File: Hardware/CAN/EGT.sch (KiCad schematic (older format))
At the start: 1 part

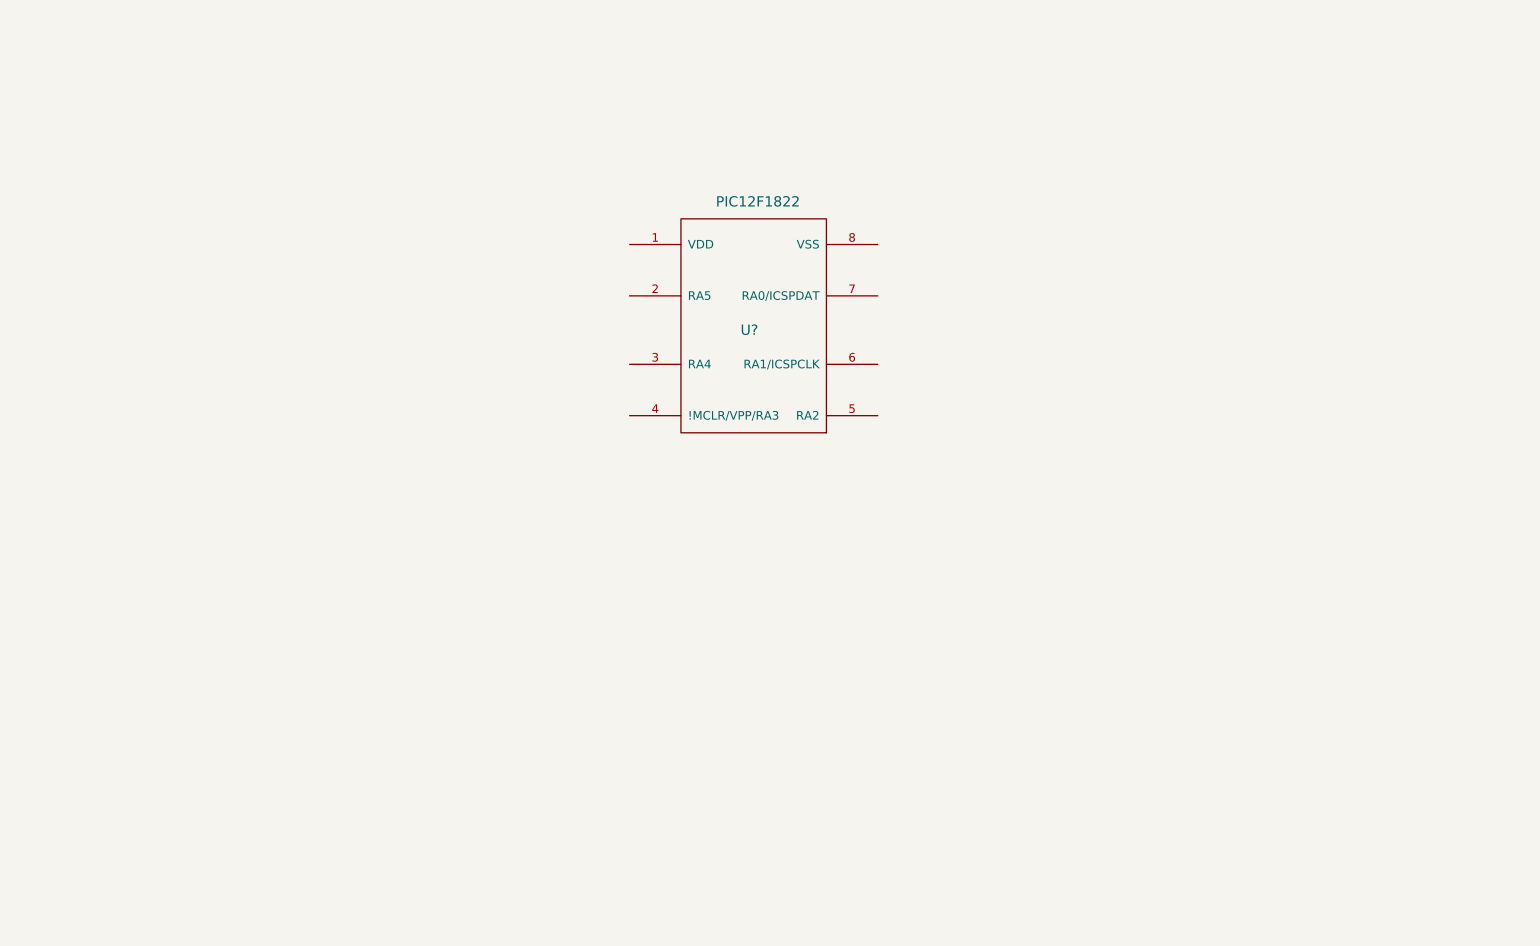
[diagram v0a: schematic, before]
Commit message: Added components, library
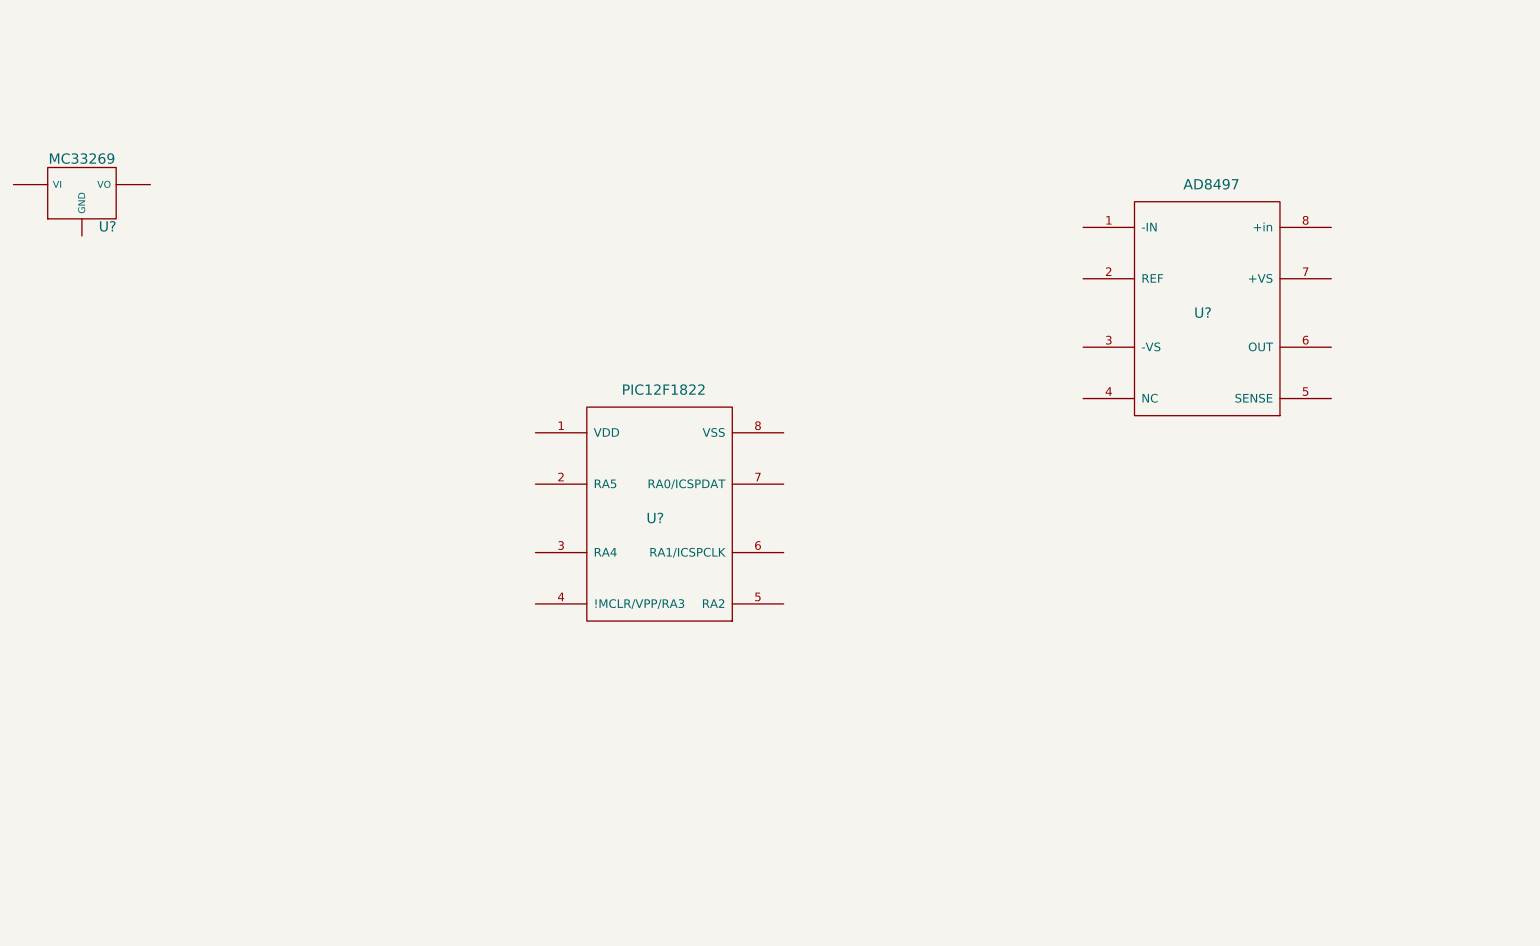
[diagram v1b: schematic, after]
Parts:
- added U?: MC33269, ~, symbol MC33269
- added U?: AD8497, ~, symbol AD8497
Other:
- moved on the sheet: U?
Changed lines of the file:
@@
 LIBS:contrib
 LIBS:valves
-LIBS:EGT-cache
 EELAYER 27 0
 EELAYER END
@@
 L PIC12F1822 U?
 U 1 1 51C7BBAD
-P 6400 3150
-F 0 "U?" H 6350 3150 60  0000 C CNN
-F 1 "PIC12F1822" H 6400 3900 60  0000 C CNN
-F 2 "" H 6400 3150 60  0000 C CNN
-F 3 "" H 6400 3150 60  0000 C CNN
-	1    6400 3150
+P 5850 4250
+F 0 "U?" H 5800 4250 60  0000 C CNN
+F 1 "PIC12F1822" H 5850 5000 60  0000 C CNN
+F 2 "" H 5850 4250 60  0000 C CNN
+F 3 "" H 5850 4250 60  0000 C CNN
+	1    5850 4250
 	1    0    0    -1
 $EndComp
+$Comp
+L MC33269 U?
+U 1 1 51C7C963
+P 2450 2350
+F 0 "U?" H 2600 2154 60  0000 C CNN
+F 1 "MC33269" H 2450 2550 60  0000 C CNN
+F 2 "~" H 2450 2350 60  0000 C CNN
+F 3 "~" H 2450 2350 60  0000 C CNN
+	1    2450 2350
+	1    0    0    -1
+$EndComp
+$Comp
+L AD8497 U?
+U 1 1 51C7CB48
+P 9050 3050
+F 0 "U?" H 9000 3050 60  0000 C CNN
+F 1 "AD8497" H 9050 3800 60  0000 C CNN
+F 2 "~" H 9050 3050 60  0000 C CNN
+F 3 "~" H 9050 3050 60  0000 C CNN
+	1    9050 3050
+	1    0    0    -1
+$EndComp

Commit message: Schematic work
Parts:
- removed U?: PIC12F1822, symbol PIC12F1822
- removed U?: AD8497, ~, symbol AD8497
- added C1, C2: 10uF, ~, symbol CAPAPOL
- added C? (x6): C, ~, symbol C
- added D1: SCHOTTKY, ~, symbol DIODESCH
- added P?: CONN_4, symbol CONN_4
- added P?: CONN_2, symbol CONN_2
- added R? (x7): R, ~, symbol R
- added U?: PIC12F1840, ~, symbol PIC12F1840
- added U?: AD8628, ~, symbol AD8628
- added U?: TJA1051TK/3, ~, symbol TJA1051TK/3
- gave numbers to parts that had none: 1
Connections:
- net at VR1.GND: now also C1.2, C2.2, C?.2, C?.2, C?.2, C?.2, C?.2, P?.2 (P2), R?.2, R?.2, U?.2 (GND), U?.4 (V-), U?.8 (S), U?.8 (VSS)
- net at VR1.VI: now also C1.1, D1.2 (K)
- net at VR1.VO: now also C2.1, C?.1, R?.1, U?.1 (VDD), U?.3 (VCC), U?.5 (VIO), U?.8 (V+)
- new net: U?.2 (RA5), U?.4 (RXD)
- new net: U?.1 (TXD), U?.3 (RA4)
- new net: C?.1, R?.1, R?.2, U?.4 (!MCLR/VPP/RA3)
- new net: C?.1, R?.2, U?.5 (RA2)
- new net: R?.1, R?.2, U?.1
- new net: C?.1, C?.2, R?.1, R?.2, U?.2 (_)
- new net: C?.1, C?.1, R?.1, R?.2, U?.3 (+)
- new net: P?.3 (P3), U?.6 (CANL)
- new net: P?.4 (P4), U?.7 (CANH)
- new net: D1.1 (A), P?.1 (P1)
- new net: P?.1 (P1), R?.1
- new net: P?.2 (PM), R?.1
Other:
- moved on the sheet: VR1

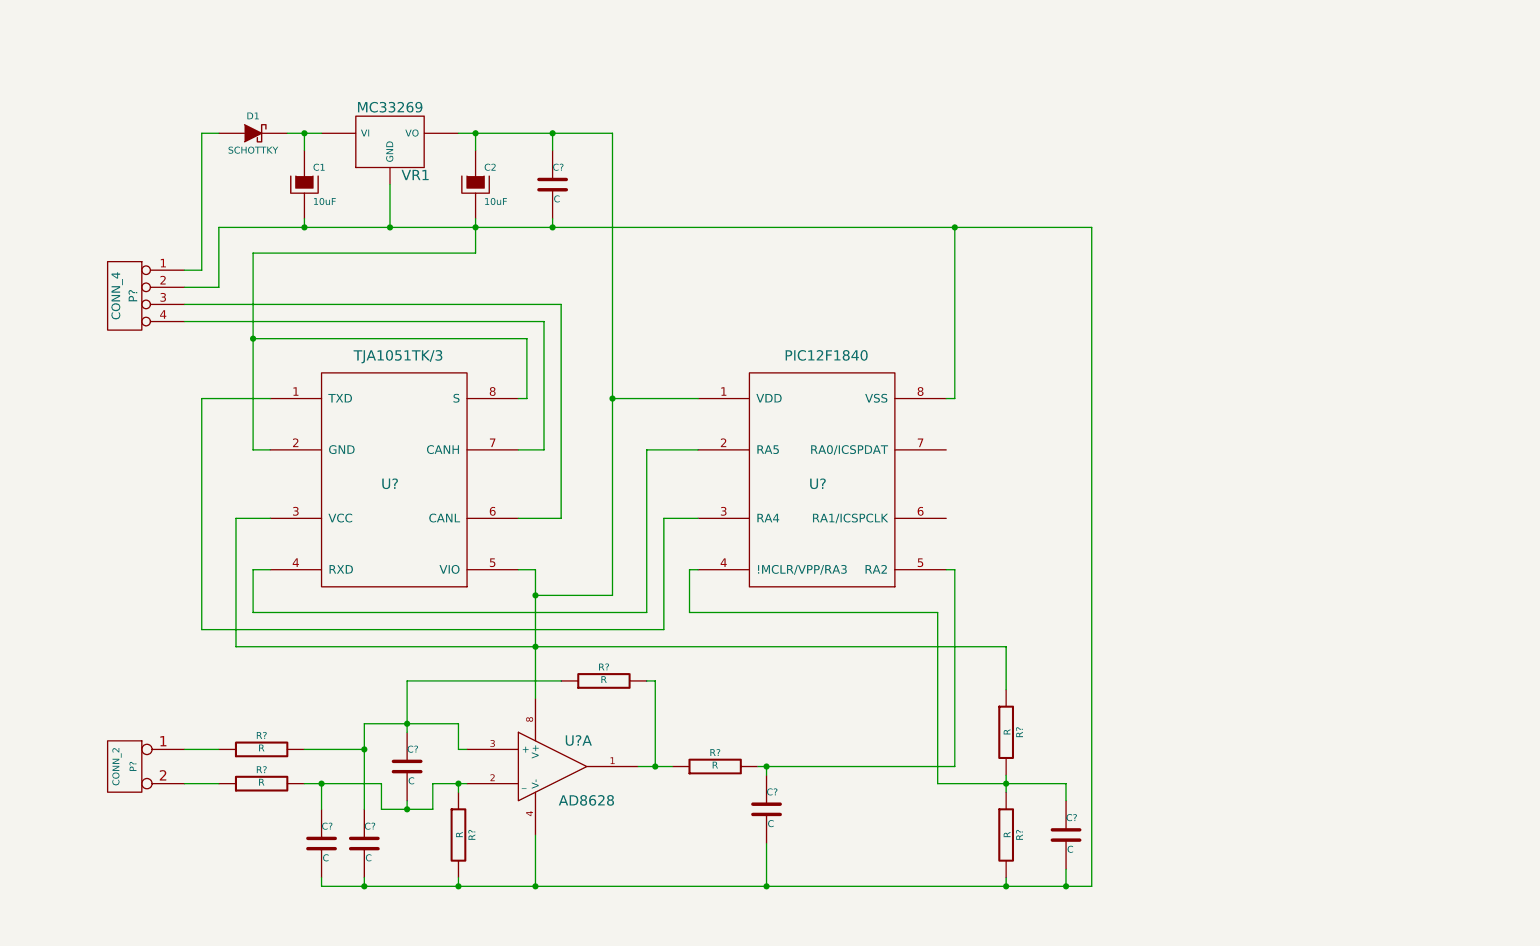
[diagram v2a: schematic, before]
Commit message: Preliminary schematic, test board layout
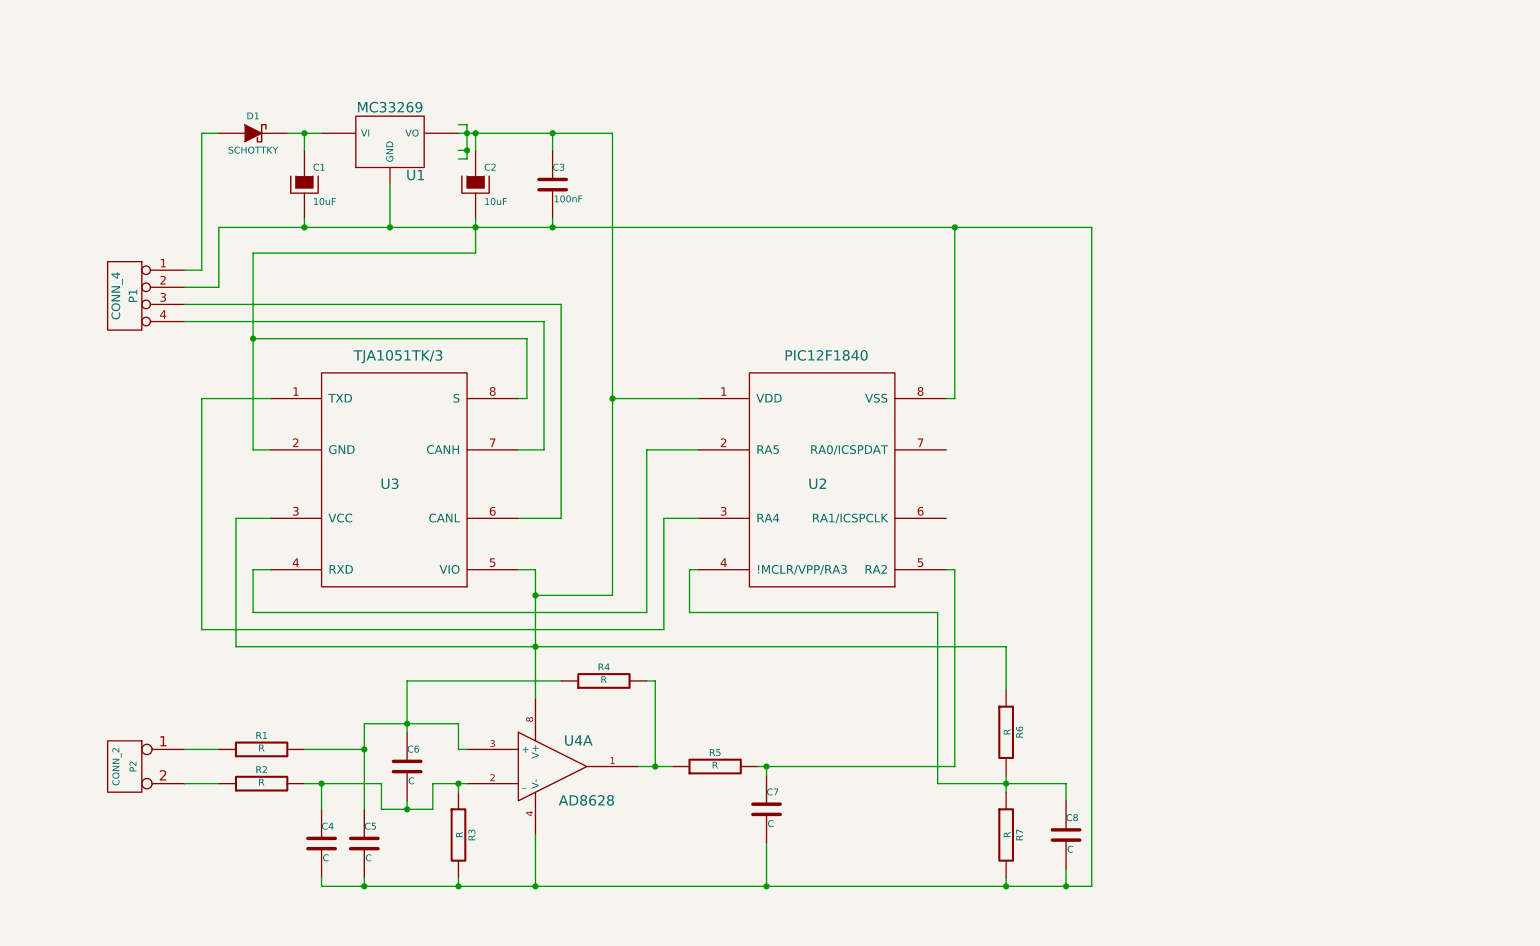
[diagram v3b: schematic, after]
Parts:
- removed VR1: MC33269, ~, symbol MC33269
- added U1: MC33269, so-8, symbol MC33269
- C1: footprint ~ -> c_tant_A; Part Number 293D106X9016A2TE3 -> F951E106MAAAQ2
- C2: footprint ~ -> c_tant_A
- C3: renamed from C?; value C -> 100nF; footprint ~ -> c_0805
- C4, C5, C6, C7, C8: renamed from C?; footprint ~ -> c_0805
- D1: footprint ~ -> SOD-123
- P1: renamed from P?; footprint (none) -> EGT_connector
- P2: renamed from P?; footprint (none) -> EGT_thermo
- R1, R2, R3, R4, R5, R6, R7: renamed from R?; footprint ~ -> c_0805
- U2, U3: renamed from U?; footprint ~ -> dfn8
- U4: renamed from U?; footprint ~ -> SOT23-5
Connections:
- wire segments 88 -> 92
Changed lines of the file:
@@
 LIBS:eregulators
 LIBS:eanalogdevices
-LIBS:EGT-cache
 EELAYER 27 0
 EELAYER END
@@
 Sheet 1 1
 Title ""
-Date "2 jul 2013"
+Date "3 jul 2013"
 Rev ""
 Comp ""
@@
 $EndDescr
 $Comp
-L MC33269 VR1
-U 1 1 51C7C963
-P 4250 2050
-F 0 "VR1" H 4400 1854 60  0000 C CNN
-F 1 "MC33269" H 4250 2250 60  0000 C CNN
-F 2 "~" H 4250 2050 60  0000 C CNN
-F 3 "~" H 4250 2050 60  0000 C CNN
-	1    4250 2050
-	1    0    0    -1
-$EndComp
-$Comp
-L PIC12F1840 U?
+L PIC12F1840 U2
 U 1 1 51D2DDA0
 P 6800 4050
-F 0 "U?" H 6750 4050 60  0000 C CNN
+F 0 "U2" H 6750 4050 60  0000 C CNN
 F 1 "PIC12F1840" H 6800 4800 60  0000 C CNN
-F 2 "~" H 6800 4050 60  0000 C CNN
+F 2 "dfn8" H 6800 4050 60  0001 C CNN
 F 3 "~" H 6800 4050 60  0000 C CNN
 	1    6800 4050
@@
 $EndComp
 $Comp
-L AD8628 U?
+L AD8628 U4
 U 1 1 51D2E39A
 P 5200 5700
-F 0 "U?" H 5350 5850 60  0000 C CNN
+F 0 "U4" H 5350 5850 60  0000 C CNN
 F 1 "AD8628" H 5400 5500 60  0000 C CNN
-F 2 "~" H 5200 5700 60  0000 C CNN
+F 2 "SOT23-5" H 5200 5700 60  0001 C CNN
 F 3 "~" H 5200 5700 60  0000 C CNN
 	1    5200 5700
@@
 $EndComp
 $Comp
-L TJA1051TK/3 U?
+L TJA1051TK/3 U3
 U 1 1 51D2E563
 P 4300 4050
-F 0 "U?" H 4250 4050 60  0000 C CNN
+F 0 "U3" H 4250 4050 60  0000 C CNN
 F 1 "TJA1051TK/3" H 4300 4800 60  0000 C CNN
-F 2 "~" H 4300 4050 60  0000 C CNN
+F 2 "dfn8" H 4300 4050 60  0001 C CNN
 F 3 "~" H 4300 4050 60  0000 C CNN
 	1    4300 4050
@@
 F 0 "C2" H 4800 2400 40  0000 L CNN
 F 1 "10uF" H 4800 2200 40  0000 L CNN
-F 2 "~" H 4850 2150 30  0000 C CNN
+F 2 "c_tant_A" H 4850 2150 30  0001 C CNN
 F 3 "~" H 4750 2300 300 0000 C CNN
 F 4 "293D106X9016A2TE3" H 4750 2300 60  0001 C CNN "Part Number"
@@
 F 0 "D1" H 3450 2100 40  0000 C CNN
 F 1 "SCHOTTKY" H 3450 1900 40  0000 C CNN
-F 2 "~" H 3450 2000 60  0000 C CNN
+F 2 "SOD-123" H 3450 2000 60  0001 C CNN
 F 3 "~" H 3450 2000 60  0000 C CNN
 F 4 "MBR0530" H 3450 2000 60  0001 C CNN "Part Number"
@@
 	3250 2550 8350 2550
 $Comp
-L CONN_4 P?
+L CONN_4 P1
 U 1 1 51D31415
 P 2700 2950
-F 0 "P?" V 2650 2950 50  0000 C CNN
+F 0 "P1" V 2650 2950 50  0000 C CNN
 F 1 "CONN_4" V 2750 2950 50  0000 C CNN
-F 2 "" H 2700 2950 60  0000 C CNN
+F 2 "EGT_connector" H 2700 2950 60  0001 C CNN
 F 3 "" H 2700 2950 60  0000 C CNN
 	1    2700 2950
@@
 	5250 3000 3050 3000
 $Comp
-L CONN_2 P?
+L CONN_2 P2
 U 1 1 51D3193F
 P 2700 5700
-F 0 "P?" V 2650 5700 40  0000 C CNN
+F 0 "P2" V 2650 5700 40  0000 C CNN
 F 1 "CONN_2" V 2750 5700 40  0000 C CNN
-F 2 "" H 2700 5700 60  0000 C CNN
+F 2 "EGT_thermo" H 2700 5700 60  0001 C CNN
 F 3 "" H 2700 5700 60  0000 C CNN
 	1    2700 5700
@@
 $EndComp
 $Comp
-L R R?
+L R R1
 U 1 1 51D337AC
 P 3500 5600
-F 0 "R?" V 3580 5600 40  0000 C CNN
+F 0 "R1" V 3580 5600 40  0000 C CNN
 F 1 "R" V 3507 5601 40  0000 C CNN
-F 2 "~" V 3430 5600 30  0000 C CNN
+F 2 "c_0805" V 3430 5600 30  0001 C CNN
 F 3 "~" H 3500 5600 30  0000 C CNN
 	1    3500 5600
@@
 $EndComp
 $Comp
-L R R?
+L R R4
 U 1 1 51D337BB
 P 5500 5200
-F 0 "R?" V 5580 5200 40  0000 C CNN
+F 0 "R4" V 5580 5200 40  0000 C CNN
 F 1 "R" V 5507 5201 40  0000 C CNN
-F 2 "~" V 5430 5200 30  0000 C CNN
+F 2 "c_0805" V 5430 5200 30  0001 C CNN
 F 3 "~" H 5500 5200 30  0000 C CNN
 	1    5500 5200
@@
 $EndComp
 $Comp
-L R R?
+L R R2
 U 1 1 51D337CA
 P 3500 5800
-F 0 "R?" V 3580 5800 40  0000 C CNN
+F 0 "R2" V 3580 5800 40  0000 C CNN
 F 1 "R" V 3507 5801 40  0000 C CNN
-F 2 "~" V 3430 5800 30  0000 C CNN
+F 2 "c_0805" V 3430 5800 30  0001 C CNN
 F 3 "~" H 3500 5800 30  0000 C CNN
 	1    3500 5800
@@
 $EndComp
 $Comp
-L R R?
+L R R3
 U 1 1 51D337D9
 P 4650 6100
-F 0 "R?" V 4730 6100 40  0000 C CNN
+F 0 "R3" V 4730 6100 40  0000 C CNN
 F 1 "R" V 4657 6101 40  0000 C CNN
-F 2 "~" V 4580 6100 30  0000 C CNN
+F 2 "c_0805" V 4580 6100 30  0001 C CNN
 F 3 "~" H 4650 6100 30  0000 C CNN
 	1    4650 6100
@@
 $EndComp
 $Comp
-L R R?
+L R R6
 U 1 1 51D337E8
 P 7850 5500
-F 0 "R?" V 7930 5500 40  0000 C CNN
+F 0 "R6" V 7930 5500 40  0000 C CNN
 F 1 "R" V 7857 5501 40  0000 C CNN
-F 2 "~" V 7780 5500 30  0000 C CNN
+F 2 "c_0805" V 7780 5500 30  0001 C CNN
 F 3 "~" H 7850 5500 30  0000 C CNN
 	1    7850 5500
@@
 $EndComp
 $Comp
-L R R?
+L R R5
 U 1 1 51D337F7
 P 6150 5700
-F 0 "R?" V 6230 5700 40  0000 C CNN
+F 0 "R5" V 6230 5700 40  0000 C CNN
 F 1 "R" V 6157 5701 40  0000 C CNN
-F 2 "~" V 6080 5700 30  0000 C CNN
+F 2 "c_0805" V 6080 5700 30  0001 C CNN
 F 3 "~" H 6150 5700 30  0000 C CNN
 	1    6150 5700
@@
 $EndComp
 $Comp
-L C C?
+L C C5
 U 1 1 51D33806
 P 4100 6150
-F 0 "C?" H 4100 6250 40  0000 L CNN
+F 0 "C5" H 4100 6250 40  0000 L CNN
 F 1 "C" H 4106 6065 40  0000 L CNN
-F 2 "~" H 4138 6000 30  0000 C CNN
+F 2 "c_0805" H 4138 6000 30  0001 C CNN
 F 3 "~" H 4100 6150 60  0000 C CNN
 	1    4100 6150
@@
 $EndComp
 $Comp
-L C C?
+L C C4
 U 1 1 51D3381A
 P 3850 6150
-F 0 "C?" H 3850 6250 40  0000 L CNN
+F 0 "C4" H 3850 6250 40  0000 L CNN
 F 1 "C" H 3856 6065 40  0000 L CNN
-F 2 "~" H 3888 6000 30  0000 C CNN
+F 2 "c_0805" H 3888 6000 30  0001 C CNN
 F 3 "~" H 3850 6150 60  0000 C CNN
 	1    3850 6150
@@
 $EndComp
 $Comp
-L C C?
+L C C6
 U 1 1 51D33829
 P 4350 5700
-F 0 "C?" H 4350 5800 40  0000 L CNN
+F 0 "C6" H 4350 5800 40  0000 L CNN
 F 1 "C" H 4356 5615 40  0000 L CNN
-F 2 "~" H 4388 5550 30  0000 C CNN
+F 2 "c_0805" H 4388 5550 30  0001 C CNN
 F 3 "~" H 4350 5700 60  0000 C CNN
 	1    4350 5700
@@
 $EndComp
 $Comp
-L C C?
+L C C7
 U 1 1 51D33838
 P 6450 5950
-F 0 "C?" H 6450 6050 40  0000 L CNN
+F 0 "C7" H 6450 6050 40  0000 L CNN
 F 1 "C" H 6456 5865 40  0000 L CNN
-F 2 "~" H 6488 5800 30  0000 C CNN
+F 2 "c_0805" H 6488 5800 30  0001 C CNN
 F 3 "~" H 6450 5950 60  0000 C CNN
 	1    6450 5950
@@
 Connection ~ 5100 6400
 $Comp
-L C C?
+L C C8
 U 1 1 51D33E71
 P 8200 6100
-F 0 "C?" H 8200 6200 40  0000 L CNN
+F 0 "C8" H 8200 6200 40  0000 L CNN
 F 1 "C" H 8206 6015 40  0000 L CNN
-F 2 "~" H 8238 5950 30  0000 C CNN
+F 2 "c_0805" H 8238 5950 30  0001 C CNN
 F 3 "~" H 8200 6100 60  0000 C CNN
 	1    8200 6100
@@
 $EndComp
 $Comp
-L R R?
+L R R7
 U 1 1 51D33E80
 P 7850 6100
-F 0 "R?" V 7930 6100 40  0000 C CNN
+F 0 "R7" V 7930 6100 40  0000 C CNN
 F 1 "R" V 7857 6101 40  0000 C CNN
-F 2 "~" V 7780 6100 30  0000 C CNN
+F 2 "c_0805" V 7780 6100 30  0001 C CNN
 F 3 "~" H 7850 6100 30  0000 C CNN
 	1    7850 6100
@@
 F 0 "C1" H 3800 2400 40  0000 L CNN
 F 1 "10uF" H 3800 2200 40  0000 L CNN
-F 2 "~" H 3850 2150 30  0000 C CNN
+F 2 "c_tant_A" H 3850 2150 30  0001 C CNN
 F 3 "~" H 3750 2300 300 0000 C CNN
-F 4 "293D106X9016A2TE3" H 3750 2300 60  0001 C CNN "Part Number"
+F 4 "F951E106MAAAQ2" H 3750 2300 60  0001 C CNN "Part Number"
 	1    3750 2300
 	1    0    0    -1
@@
 	3350 4250 3350 5000
 $Comp
-L C C?
+L C C3
 U 1 1 51D34781
 P 5200 2300
-F 0 "C?" H 5200 2400 40  0000 L CNN
-F 1 "C" H 5206 2215 40  0000 L CNN
-F 2 "~" H 5238 2150 30  0000 C CNN
+F 0 "C3" H 5200 2400 40  0000 L CNN
+F 1 "100nF" H 5206 2215 40  0000 L CNN
+F 2 "c_0805" H 5238 2150 30  0001 C CNN
 F 3 "~" H 5200 2300 60  0000 C CNN
 	1    5200 2300
@@
 	5050 3200 3450 3200
 Connection ~ 3450 3200
+$Comp
+L MC33269 U1
+U 1 1 51D38633
+P 4250 2050
+F 0 "U1" H 4400 1854 60  0000 C CNN
+F 1 "MC33269" H 4250 2250 60  0000 C CNN
+F 2 "so-8" H 4250 2050 60  0001 C CNN
+F 3 "~" H 4250 2050 60  0000 C CNN
+	1    4250 2050
+	1    0    0    -1
+$EndComp
+Wire Wire Line
+	4650 1950 4700 1950
+Wire Wire Line
+	4700 1950 4700 2150
+Connection ~ 4700 2000
+Wire Wire Line
+	4700 2100 4650 2100
+Wire Wire Line
+	4700 2150 4650 2150
+Connection ~ 4700 2100
 $EndSCHEMATC

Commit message: Revised Op Amp choice, added analog and digital output.  Added ISCP Connector
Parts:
- removed P1: CONN_4, EGT_connector, symbol CONN_4
- removed U4: AD8628, SOT23-5, symbol AD8628
- added C9: C, c_0402, symbol C
- added D2, D3: DIODESCH, ~, symbol DIODESCH
- added K1: CONN_3, symbol CONN_3
- added P1: CONN_3X2, symbol CONN_3X2
- added R10, R11, R8, R9: R, c_0402, symbol R
- added U4: OPA2727, dfn8, symbol OPA2727
- C4, C5, C6, C7, C8, R1, R2, R3, R4, R6, R7: footprint c_0805 -> c_0402
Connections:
- wire segments 92 -> 124
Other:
- moved on the sheet: C1, C2, C3, C4, C5, C6, C7, C8, D1, P2, R1, R2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
